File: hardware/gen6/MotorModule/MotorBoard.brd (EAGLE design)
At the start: 61 x 50.1 mm, 42 parts, among them J1 M20X2SHROUDED

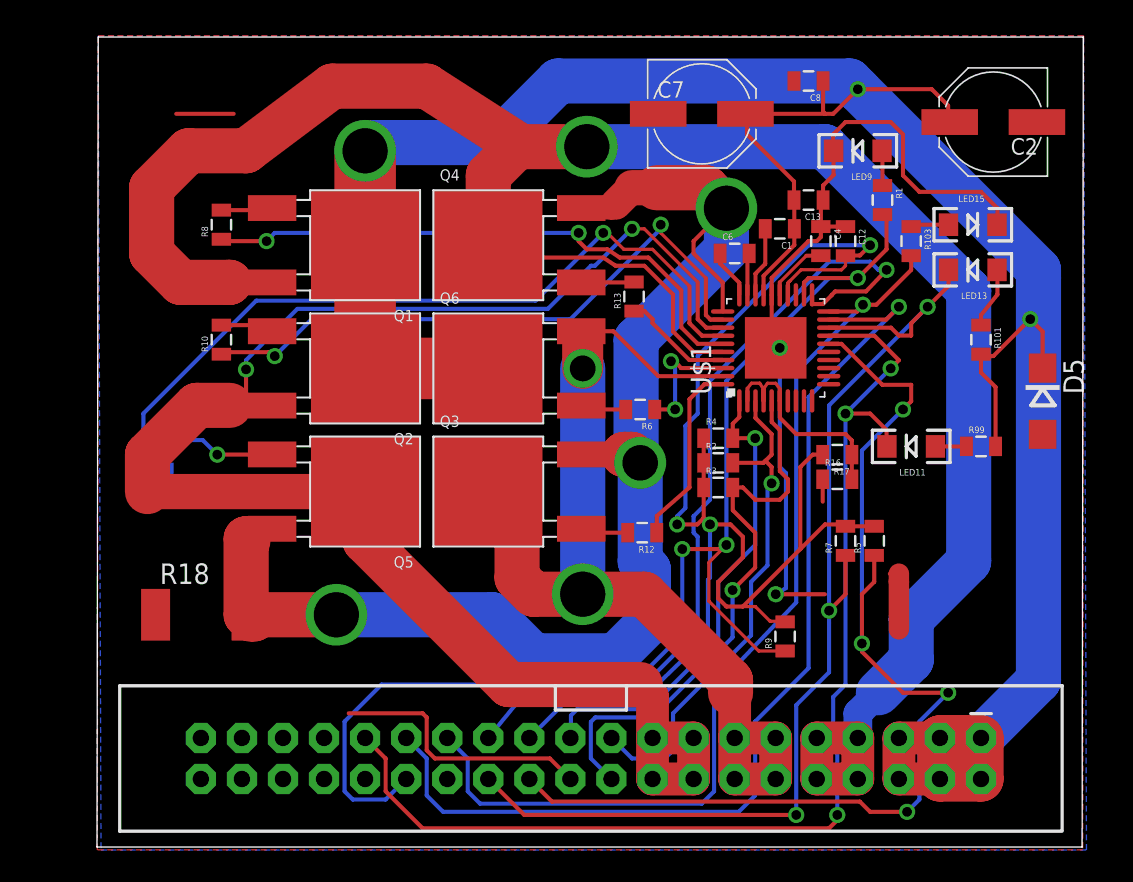
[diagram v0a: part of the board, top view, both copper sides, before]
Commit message: new motor controller
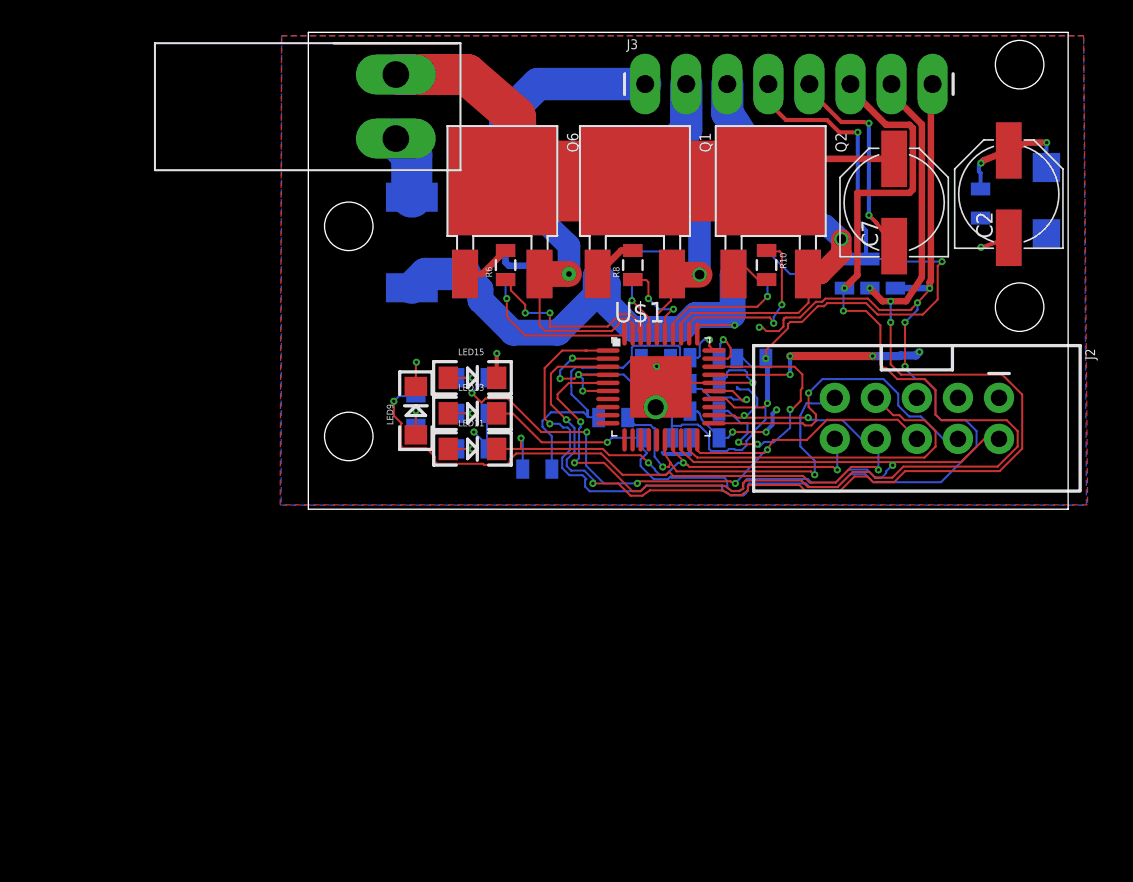
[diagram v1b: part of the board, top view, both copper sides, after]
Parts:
- removed J1: M20X2SHROUDED, SparkFun-Connectors:2X20_SHROUDED
- added J2: (no value), SparkFun-Connectors:2X5-SHROUDED
- added J3: (no value), SparkFun-Connectors:1X08_LONGPADS
- added U$2: POWER_CONN_2X1, Kicker:POWER_CONN_2X1
- R9: value 0 -> 10k
- moved R14 39.1 mm to (41.3, 35.6)
- moved R10 34.0 mm to (41.3, 35.6), turned to 270 degrees
- moved LED15 32.4 mm to (23.2, 28.6)
- moved LED13 32.2 mm to (23.2, 26.4), turned to 0 degrees
- moved R101 31.8 mm to (23.2, 26.4), flipped to the bottom, turned to 180 degrees
- moved LED9 31.7 mm to (19.7, 26.6), turned to 90 degrees
- moved R1 31.7 mm to (19.7, 26.6), flipped to the bottom, turned to 90 degrees
- moved Q5 31.6 mm to (41.6, 40.8), flipped to the bottom, turned to 270 degrees
- moved R99 31.5 mm to (23.2, 24.2), flipped to the bottom, turned to 180 degrees
- moved R103 28.4 mm to (23.2, 28.6), flipped to the bottom, turned to 180 degrees
- moved Q2 27.6 mm to (41.6, 40.8), turned to 270 degrees
- moved LED11 27.1 mm to (23.2, 24.2), turned to 0 degrees
- moved R18 26.5 mm to (19.4, 37.0), flipped to the bottom, turned to 270 degrees
- moved R8 25.6 mm to (33.1, 35.6)
- moved Q3 19.2 mm to (25.0, 40.8), flipped to the bottom, turned to 270 degrees
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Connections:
- net 12V: now also U$2.+; no longer J1.1, J1.2, J1.3, J1.4, J1.5, J1.6
- net 5V: now also J3.4; no longer J1.23
- net BRAKE: now also J2.6; no longer J1.27
- net DIR: now also J2.4; no longer J1.25
- net ENABLE: now also J2.8; no longer J1.30, R9.1
- net FAULTN: now also J2.10, R9.1; no longer J1.31
- net GND: now also J2.1, J3.5, U$2.-; no longer J1.22, J1.33, J1.34, J1.35, J1.36, J1.37, J1.38, J1.39, J1.40
- net HALLOUT: now also J2.9; no longer J1.24
- net LOCKN: now also J2.2; no longer J1.26
- net M1H1: now also J3.6; no longer J1.20
- net M1H2: now also J3.7; no longer J1.19
- net M1H3: now also J3.8; no longer J1.21
- net M1O1: now also J3.1; no longer J1.11, J1.12, J1.13, J1.14
- net M1O2: now also J3.2; no longer J1.10, J1.7, J1.8, J1.9
- net M1O3: now also J3.3; no longer J1.15, J1.16, J1.17, J1.18
- net PWM: now also J2.7; no longer J1.29
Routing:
- net M1O2: track 136.2 -> 22.0 mm
- net 12V: track 166.4 -> 73.6 mm, vias 3 -> 10
- net M1O3: track 101.8 -> 26.8 mm, vias 2 -> 1
- net M1H3: track 29.7 -> 81.2 mm, vias 1 -> 6
- net O1: track 84.3 -> 35.9 mm, vias 3 -> 1
- net HALLOUT: track 68.7 -> 22.9 mm, vias 4 -> 2
- net M1H2: track 31.5 -> 75.6 mm, vias 1 -> 5
- net FAULTN: track 72.1 -> 29.0 mm, vias 3 -> 4
- net PWM: track 63.8 -> 21.8 mm, vias 1 -> 0
- net N$17: track 48.8 -> 8.26 mm
- net M1H1: track 35.6 -> 76.0 mm, vias 1 -> 4
- net GND: track 77.3 -> 42.3 mm, vias 2 -> 8
- net DIR: track 51.6 -> 20.0 mm
- net N$20: track 35.9 -> 5.65 mm
- net M1O1: track 61.9 -> 33.6 mm, vias 2 -> 1
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- added copper zone on layer 1, net 12V
- removed copper zone on layer 1, net GND
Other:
- board size 61 x 50.1 mm -> 47 x 29.5 mm

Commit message: started conversion
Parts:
- added C3, C5: .1uF, SparkFun-Passives:0805
- added IC1: 4011D, 40xx:SO14
- added R11, R25: 4.7k, SparkFun-Resistors:0805
- added R15, R19, R20, R21, R22: 1k, SparkFun-Resistors:0805
- added R23, R24: 10k, SparkFun-Resistors:0805
- added U1: SN74LVC1G32DCKR, SparkFun-IC-Logic:SOT23-5
- added U2: 74HC1G04, SparkFun-IC-Logic:SOT353
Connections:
- new net N$12: R11.1, R15.1
- new net N$23: R19.2
- new net N$24: R19.1
- new net N$25: U1.1, U2.2
- new net N$26: IC1.2, U2.4
- new net N$27: IC1.1, U1.2
- new net N$28: U1.4
- new net N$29: R21.2
- new net N$30: R21.1
- new net N$31: IC1.3
- new net N$32: R20.1
- new net N$33: R20.2
- new net N$34: R22.2, R23.1
- new net N$35: R23.2, R24.1
- new net N$36: R22.1, R24.2
- new net N$37: R25.2
- new net VDD: IC1.14
- new net VSS: IC1.7

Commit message: finished beginnings of schematic
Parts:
- added C10: 47uF, rcl:085CS_1AW
- added C9: .1uF, SparkFun-Passives:0805
- added LED1, LED2: (no value), led:SMARTLED-TTW
- added Q7: IRFP250, transistor-power:TO-247AD-V
- C3: value .1uF -> 33nF
- C5: value .1uF -> 47uF; device SparkFun-Passives:0805 -> rcl:085CS_1AW
- moved C5 18.1 mm to (-147.4, -13.7)
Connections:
- removed net N$33: R20.2
- new net +5V: Q7.S
- new net N$38: LED1.C@1, LED2.A@1, R25.1
- new net N$39: LED1.A@1, LED2.C@1
- net GND: now also C10.-, C3.2, C5.-, C9.1, R22.1, R24.2
- net N$35: now also C3.1, R20.2
- net N$36: now also C10.+, C5.+, C9.2, Q7.D; no longer R22.1, R24.2
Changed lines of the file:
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@@
 <attribute name="VALUE" x="-126.492" y="-6.477" size="0.4064" layer="27"/>
 </element>
-<element name="C3" library="SparkFun-Passives" package="0805" value=".1uF" x="-128.524" y="-5.08" smashed="yes">
+<element name="C3" library="SparkFun-Passives" package="0805" value="33nF" x="-128.524" y="-5.08" smashed="yes">
 <attribute name="NAME" x="-129.286" y="-4.2545" size="0.4064" layer="25"/>
 <attribute name="VALUE" x="-129.54" y="-6.477" size="0.4064" layer="27"/>
 </element>
-<element name="C5" library="SparkFun-Passives" package="0805" value=".1uF" x="-131.572" y="-5.08" smashed="yes">
-<attribute name="NAME" x="-132.334" y="-4.2545" size="0.4064" layer="25"/>
-<attribute name="VALUE" x="-132.588" y="-6.477" size="0.4064" layer="27"/>
+<element name="C9" library="SparkFun-Passives" package="0805" value=".1uF" x="-134.62" y="-5.08" smashed="yes">
+<attribute name="NAME" x="-135.382" y="-4.2545" size="0.4064" layer="25"/>
+<attribute name="VALUE" x="-135.636" y="-6.477" size="0.4064" layer="27"/>
+</element>
+<element name="LED1" library="led" library_urn="urn:adsk.eagle:library:259" package="SMARTLED-TTW" package3d_urn="urn:adsk.eagle:package:15825/1" value="" x="-138.557" y="-5.207" smashed="yes">
+<attribute name="NAME" x="-139.192" y="-6.477" size="1.27" layer="25" rot="R90"/>
+<attribute name="VALUE" x="-136.652" y="-6.477" size="1.27" layer="27" rot="R90"/>
+</element>
+<element name="LED2" library="led" library_urn="urn:adsk.eagle:library:259" package="SMARTLED-TTW" package3d_urn="urn:adsk.eagle:package:15825/1" value="" x="-143.51" y="-5.207" smashed="yes">
+<attribute name="NAME" x="-144.145" y="-6.477" size="1.27" layer="25" rot="R90"/>
+<attribute name="VALUE" x="-141.605" y="-6.477" size="1.27" layer="27" rot="R90"/>
+</element>
+<element name="C10" library="rcl" library_urn="urn:adsk.eagle:library:334" package="085CS_1AW" package3d_urn="urn:adsk.eagle:package:23385/1" value="47uF" x="-147.447" y="-5.08" smashed="yes">
+<attribute name="NAME" x="-148.209" y="-4.2545" size="0.4064" layer="25"/>
+<attribute name="SPICEPREFIX" value="C" x="-147.447" y="-5.08" size="1.778" layer="27" display="off"/>
+<attribute name="VALUE" x="-148.463" y="-6.477" size="0.4064" layer="27"/>
+</element>
+<element name="C5" library="rcl" library_urn="urn:adsk.eagle:library:334" package="085CS_1AW" package3d_urn="urn:adsk.eagle:package:23385/1" value="47uF" x="-147.447" y="-13.716" smashed="yes">
+<attribute name="NAME" x="-151.257" y="-11.176" size="1.27" layer="25"/>
+<attribute name="SPICEPREFIX" value="C" x="-147.447" y="-13.716" size="1.778" layer="27" display="off"/>
+<attribute name="VALUE" x="-151.257" y="-17.526" size="1.27" layer="27"/>
+</element>
+<element name="Q7" library="transistor-power" library_urn="urn:adsk.eagle:library:400" package="TO-247AD-V" package3d_urn="urn:adsk.eagle:package:29508/1" value="IRFP250" x="-146.177" y="-18.161" smashed="yes">
+<attribute name="NAME" x="-153.797" y="-25.846" size="1.778" layer="25" ratio="10"/>
+<attribute name="VALUE" x="-153.797" y="-27.751" size="1.778" layer="27" ratio="10"/>
 </element>
 </elements>
@@
 <wire x1="34.74993125" y1="28.21125" x2="34.74993125" y2="29.13106875" width="0.127" layer="16"/>
 <wire x1="34.74993125" y1="29.13106875" x2="34.544" y2="29.337" width="0.127" layer="16"/>
+<contactref element="R24" pad="2"/>
+<contactref element="R22" pad="1"/>
+<contactref element="C3" pad="2"/>
+<contactref element="C9" pad="1"/>
+<contactref element="C5" pad="-"/>
+<contactref element="C10" pad="-"/>
+<wire x1="-151.897" y1="-5.08" x2="-151.897" y2="-13.716" width="0" layer="19" extent="1-1"/>
+<wire x1="-135.52" y1="-5.08" x2="-151.897" y2="-5.08" width="0" layer="19" extent="1-1"/>
+<wire x1="-127.624" y1="-5.08" x2="-135.52" y2="-5.08" width="0" layer="19" extent="1-1"/>
+<wire x1="-121.528" y1="-5.08" x2="-127.624" y2="-5.08" width="0" layer="19" extent="1-1"/>
+<wire x1="-117.232" y1="-5.08" x2="-121.528" y2="-5.08" width="0" layer="19" extent="1-1"/>
+<wire x1="19.6506625" y1="28.096509375" x2="-117.232" y2="-5.08" width="0" layer="19" extent="1-1"/>
+<wire x1="24.6506625" y1="30.128509375" x2="19.685" y2="29.591" width="0" layer="19" extent="1-1"/>
+<wire x1="34.48731875" y1="27.9486375" x2="24.6506625" y2="28.628509375" width="0" layer="19" extent="1-16"/>
+<wire x1="36.607540625" y1="24.9163375" x2="34.48731875" y2="26.805403125" width="0" layer="19" extent="16-16"/>
+<wire x1="19.4" y1="39.8" x2="19.685" y2="29.591" width="0" layer="19" extent="1-16"/>
+<wire x1="49.054" y1="36.957" x2="40.513" y2="29.21" width="0" layer="19" extent="1-16"/>
+<wire x1="54.61" y1="36.703" x2="49.238" y2="36.773" width="0" layer="19" extent="1-1"/>
+<wire x1="54.582" y1="38.51" x2="54.61" y2="36.703" width="0" layer="19" extent="1-16"/>
+<wire x1="58.655" y1="37.538" x2="56.33024375" y2="37.292471875" width="0" layer="19" extent="1-16"/>
+<wire x1="55.724303125" y1="27.3907" x2="54.629" y2="36.684" width="0" layer="19" extent="1-1"/>
 </signal>
 <signal name="12V">
@@
 <contactref element="R20" pad="1"/>
 </signal>
-<signal name="N$33">
-<contactref element="R20" pad="2"/>
-</signal>
 <signal name="N$34">
 <contactref element="R23" pad="1"/>
@@
 <contactref element="R23" pad="2"/>
 <contactref element="R24" pad="1"/>
+<contactref element="C3" pad="1"/>
+<contactref element="R20" pad="2"/>
+<wire x1="-123.328" y1="-5.08" x2="-129.424" y2="-5.08" width="0" layer="19" extent="1-1"/>
 <wire x1="-118.48" y1="-5.08" x2="-123.328" y2="-5.08" width="0" layer="19" extent="1-1"/>
-</signal>
-<signal name="N$36">
-<contactref element="R24" pad="2"/>
-<contactref element="R22" pad="1"/>
-<wire x1="-117.232" y1="-5.08" x2="-121.528" y2="-5.08" width="0" layer="19" extent="1-1"/>
+<wire x1="-109.336" y1="-5.08" x2="-118.48" y2="-5.08" width="0" layer="19" extent="1-1"/>
 </signal>
 <signal name="N$37">
 <contactref element="R25" pad="2"/>
 </signal>
+<signal name="N$38">
+<contactref element="R25" pad="1"/>
+<contactref element="LED1" pad="C@1"/>
+<contactref element="LED2" pad="A@1"/>
+<wire x1="-138.557" y1="-4.707" x2="-143.51" y2="-5.707" width="0" layer="19" extent="1-1"/>
+<wire x1="-126.376" y1="-5.08" x2="-138.557" y2="-4.707" width="0" layer="19" extent="1-1"/>
+</signal>
+<signal name="N$39">
+<contactref element="LED1" pad="A@1"/>
+<contactref element="LED2" pad="C@1"/>
+<wire x1="-138.557" y1="-5.707" x2="-143.51" y2="-4.707" width="0" layer="19" extent="1-1"/>
+</signal>
+<signal name="N$36">
+<contactref element="C10" pad="+"/>
+<contactref element="C5" pad="+"/>
+<contactref element="C9" pad="2"/>
+<contactref element="Q7" pad="D"/>
+<wire x1="-142.997" y1="-13.716" x2="-146.177" y2="-20.701" width="0" layer="19" extent="1-1"/>
+<wire x1="-142.997" y1="-5.08" x2="-142.997" y2="-13.716" width="0" layer="19" extent="1-1"/>
+<wire x1="-133.72" y1="-5.08" x2="-142.997" y2="-5.08" width="0" layer="19" extent="1-1"/>
+</signal>
+<signal name="+5V">
+<contactref element="Q7" pad="S"/>
+</signal>
 </signals>

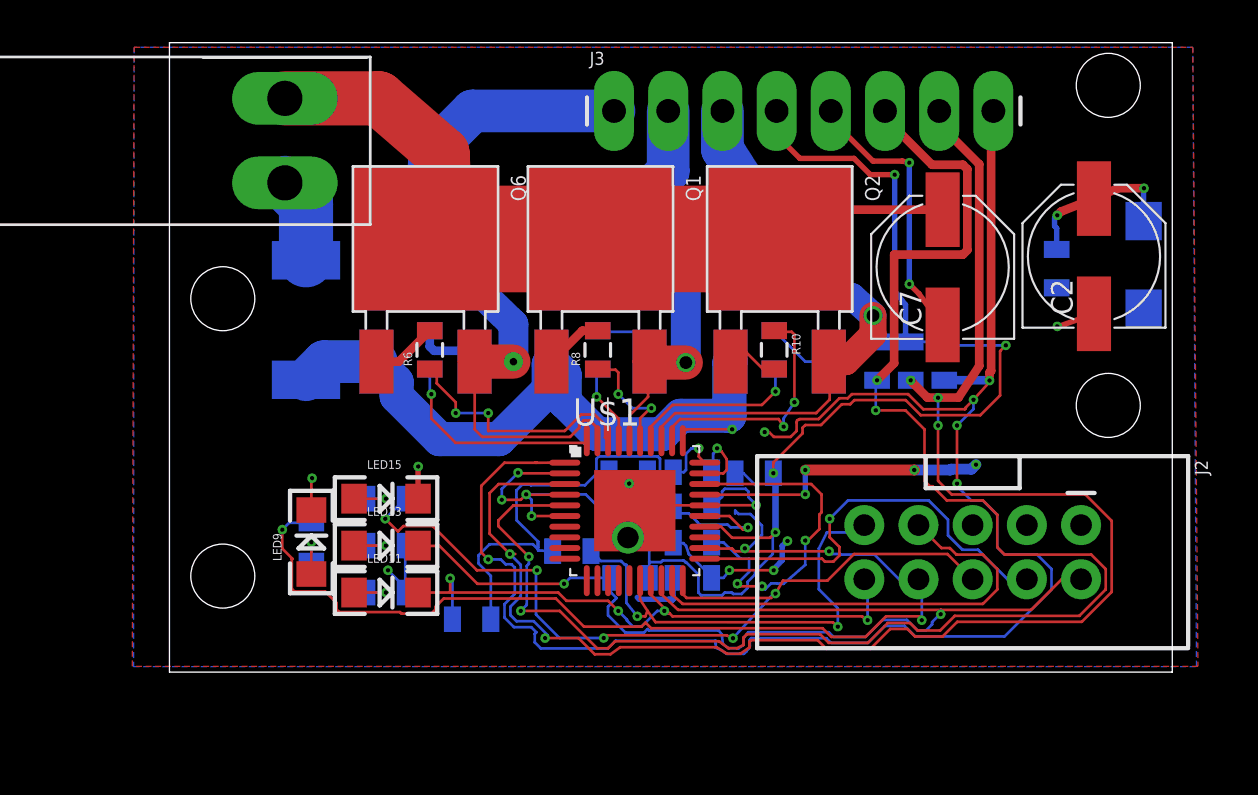
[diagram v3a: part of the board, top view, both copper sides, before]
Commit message: added VNH5019A-E package to schematic
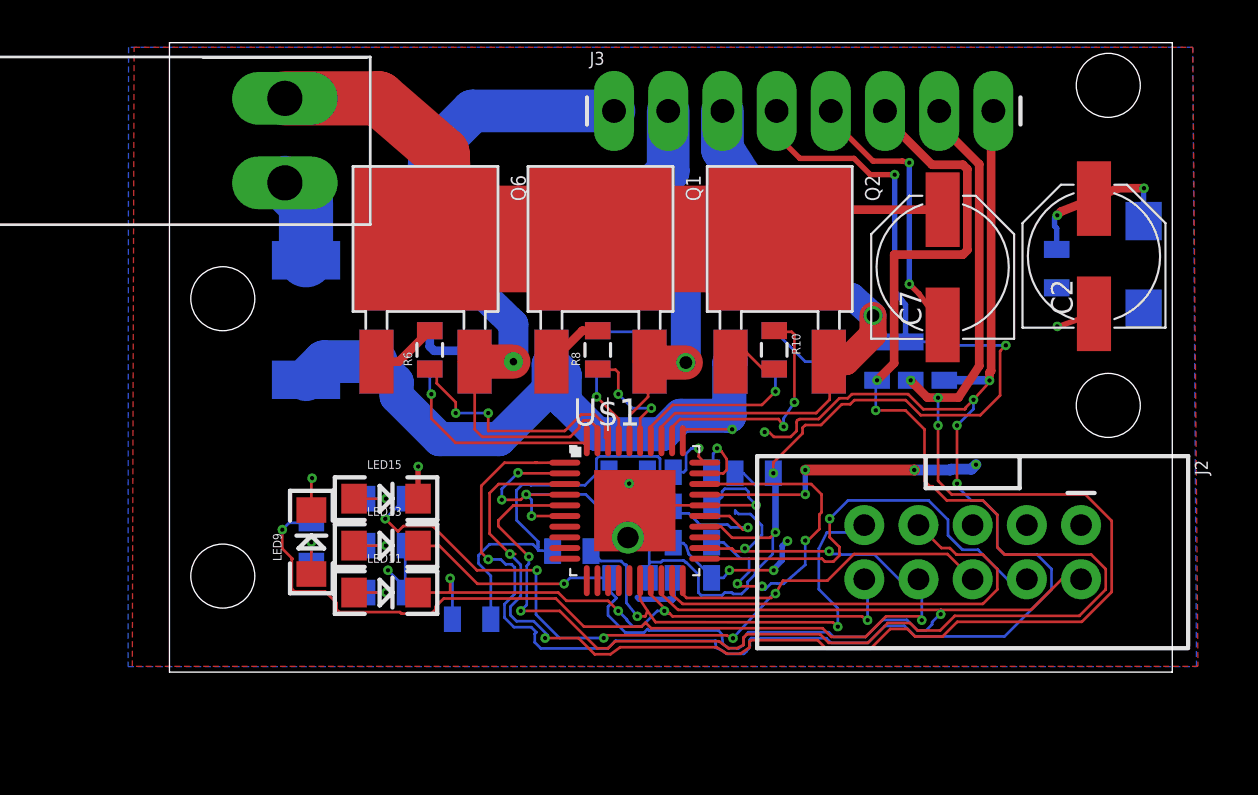
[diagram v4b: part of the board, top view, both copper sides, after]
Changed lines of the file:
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@@
 <contactref element="R18" pad="1"/>
 <polygon width="0.254" layer="16">
-<vertex x="11.343" y="49.784"/>
-<vertex x="11.31759375" y="20.7557"/>
+<vertex x="11.08333125" y="49.784"/>
+<vertex x="11.057925" y="20.7557"/>
 <vertex x="61.13459375" y="20.7557"/>
 <vertex x="60.96" y="49.784"/>
